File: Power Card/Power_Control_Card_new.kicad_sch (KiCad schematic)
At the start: 17 parts, among them J1 Conn_01x02_Pin, J4 Conn_01x04_Pin, Q1 IRF5305PbF, Q2 IRF5305PbF, U3 TSR2-2450, U4 TSR2-2433, U5 MCP9808_MSOP

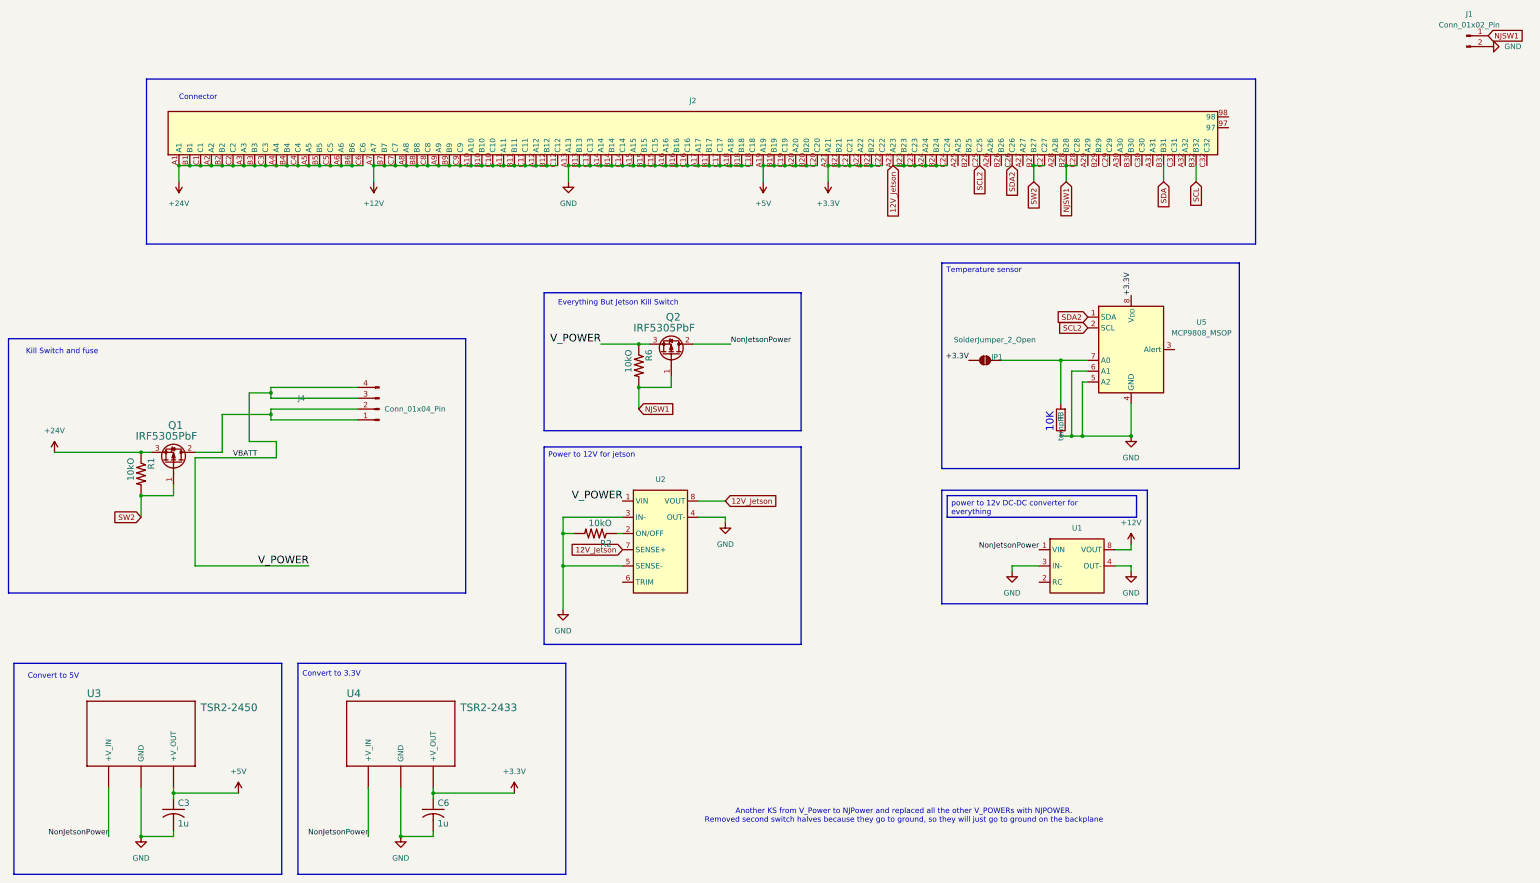
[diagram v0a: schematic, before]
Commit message: NJKS short
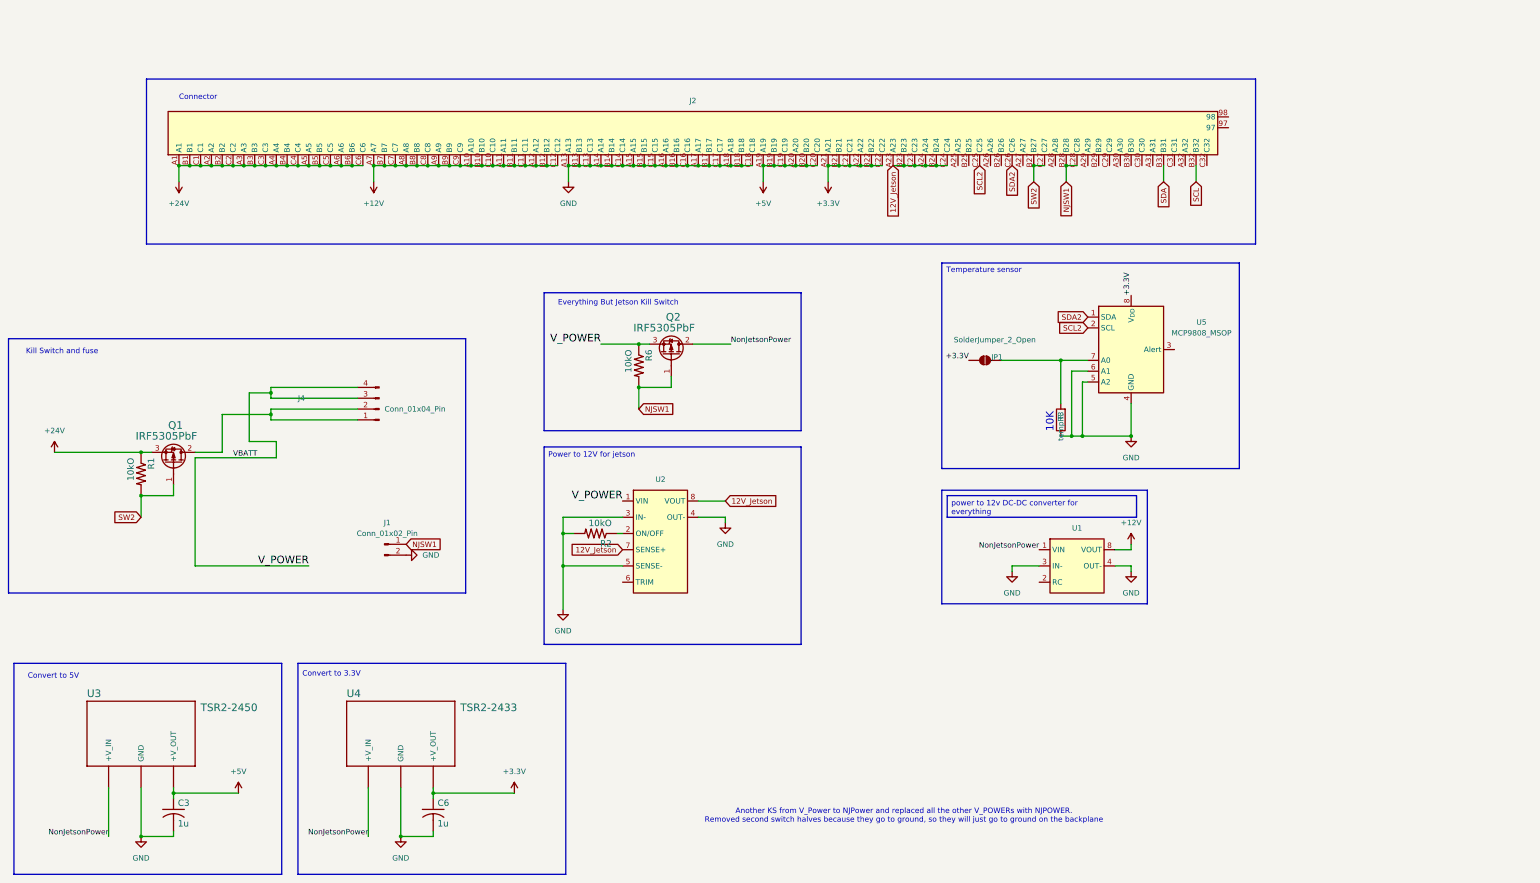
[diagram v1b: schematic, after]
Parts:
- J1: footprint (none) -> Connector_PinSocket_2.54mm:PinSocket_1x02_P2.54mm_Vertical
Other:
- moved on the sheet: J1
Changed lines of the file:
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@@
 	(global_label "NJSW1"
 		(shape input)
-		(at 369.57 60.96 0)
+		(at 115.57 180.34 0)
 		(fields_autoplaced yes)
 		(effects
@@
 		)
 		(property "Intersheetrefs" "${INTERSHEET_REFS}"
-			(at 378.7237 60.96 0)
+			(at 124.7237 180.34 0)
 			(effects
 				(font
@@
 	(symbol
 		(lib_id "Connector:Conn_01x02_Pin")
-		(at 364.49 60.96 0)
+		(at 110.49 180.34 0)
 		(unit 1)
 		(exclude_from_sim no)
@@
 		(fields_autoplaced yes)
 		(property "Reference" "J1"
-			(at 365.125 55.88 0)
+			(at 111.125 175.26 0)
 			(effects
 				(font
@@
 		)
 		(property "Value" "Conn_01x02_Pin"
-			(at 365.125 58.42 0)
-			(effects
-				(font
-					(size 1.27 1.27)
-				)
-			)
-		)
-		(property "Footprint" ""
-			(at 364.49 60.96 0)
+			(at 111.125 177.8 0)
+			(effects
+				(font
+					(size 1.27 1.27)
+				)
+			)
+		)
+		(property "Footprint" "Connector_PinSocket_2.54mm:PinSocket_1x02_P2.54mm_Vertical"
+			(at 110.49 180.34 0)
 			(effects
 				(font
@@
 		)
 		(property "Datasheet" "~"
-			(at 364.49 60.96 0)
+			(at 110.49 180.34 0)
 			(effects
 				(font
@@
 		)
 		(property "Description" "Generic connector, single row, 01x02, script generated"
-			(at 364.49 60.96 0)
+			(at 110.49 180.34 0)
 			(effects
 				(font
@@
 		(lib_name "GND_1")
 		(lib_id "power:GND")
-		(at 369.57 63.5 90)
+		(at 115.57 182.88 90)
 		(unit 1)
 		(exclude_from_sim no)
@@
 		(fields_autoplaced yes)
 		(property "Reference" "#PWR011"
-			(at 375.92 63.5 0)
+			(at 121.92 182.88 0)
 			(effects
 				(font
@@
 		)
 		(property "Value" "GND"
-			(at 373.38 63.4999 90)
+			(at 119.38 182.8799 90)
 			(effects
 				(font
@@
 		)
 		(property "Footprint" ""
-			(at 369.57 63.5 0)
+			(at 115.57 182.88 0)
 			(effects
 				(font
@@
 		)
 		(property "Datasheet" ""
-			(at 369.57 63.5 0)
+			(at 115.57 182.88 0)
 			(effects
 				(font
@@
 		)
 		(property "Description" "Power symbol creates a global label with name \"GND\" , ground"
-			(at 369.57 63.5 0)
-			(effects
-				(font
+			(at 115.57 182.88 0)
+			(effects
+				(font

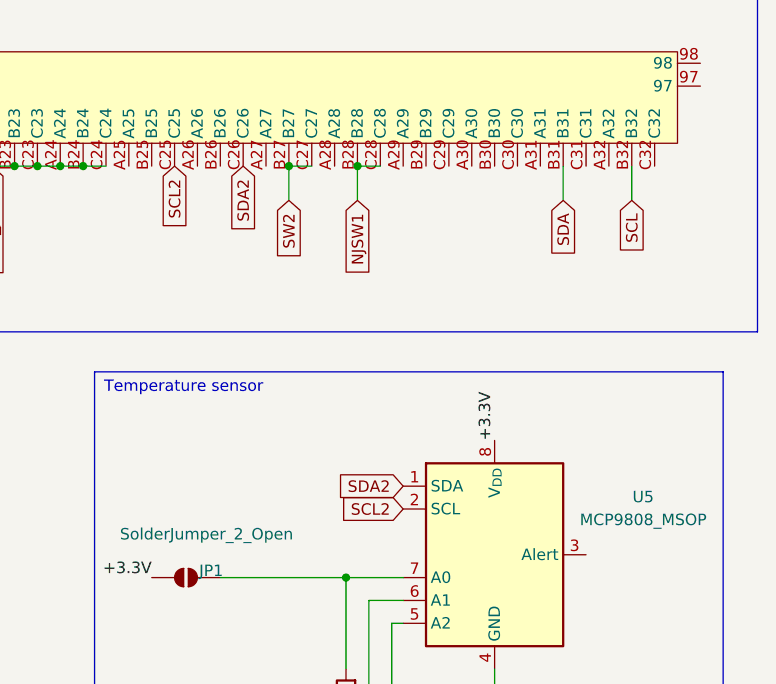
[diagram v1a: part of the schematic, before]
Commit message: Fixed the i2c line
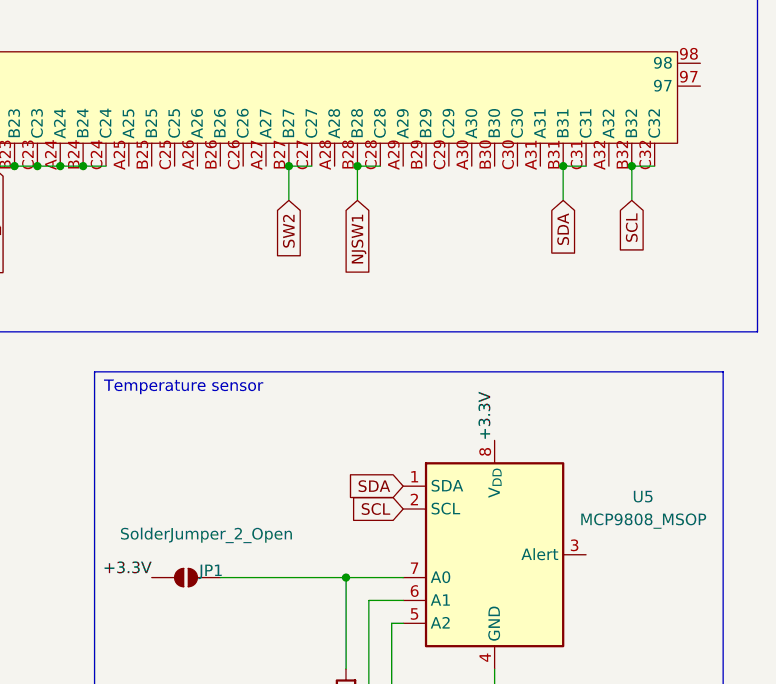
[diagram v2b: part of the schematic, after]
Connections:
- net SCL: now also J2.C32, U5.2 (SCL)
- net SDA: now also J2.C31, U5.1 (SDA)
- net SCL2: no longer names the net of J2.C25
- net SCL2: no longer U5.2 (SCL)
- net SDA2: no longer names the net of J2.C26
- net SDA2: no longer U5.1 (SDA)
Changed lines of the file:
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@@
+	)
+	(junction
+		(at 300.99 91.44)
+		(diameter 0)
+		(color 0 0 0 0)
 	)
 	(junction
@@
 	)
 	(junction
+		(at 293.37 91.44)
+		(diameter 0)
+		(color 0 0 0 0)
+	)
+	(junction
 		(at 274.32 154.94)
 		(diameter 0)
@@
 	(wire
 		(pts
+			(xy 300.99 91.44) (xy 303.53 91.44)
+		)
+		(stroke
+			(width 0)
+			(type default)
+		)
+	)
+	(wire
+		(pts
 			(xy 269.24 154.94) (xy 271.78 154.94)
+		)
+		(stroke
+			(width 0)
+			(type default)
+		)
+	)
+	(wire
+		(pts
+			(xy 293.37 91.44) (xy 295.91 91.44)
 		)
 		(stroke
@@
 	(global_label "SDA"
 		(shape input)
+		(at 275.59 127 180)
+		(fields_autoplaced yes)
+		(effects
+			(font
+				(size 1.27 1.27)
+			)
+			(justify right)
+		)
+		(property "Intersheetrefs" "${INTERSHEET_REFS}"
+			(at 269.0367 127 0)
+			(effects
+				(font
+					(size 1.27 1.27)
+				)
+				(justify right)
+				(hide yes)
+			)
+		)
+	)
+	(global_label "SDA"
+		(shape input)
 		(at 293.37 95.25 270)
 		(fields_autoplaced yes)
@@
 		)
 	)
-	(global_label "SDA2"
-		(shape input)
-		(at 275.59 127 180)
-		(fields_autoplaced yes)
-		(effects
-			(font
-				(size 1.27 1.27)
-			)
-			(justify right)
-		)
-		(property "Intersheetrefs" "${INTERSHEET_REFS}"
-			(at 267.8272 127 0)
-			(effects
-				(font
-					(size 1.27 1.27)
-				)
-				(justify right)
-				(hide yes)
-			)
-		)
-	)
-	(global_label "SCL2"
-		(shape input)
-		(at 250.19 91.44 270)
-		(fields_autoplaced yes)
-		(effects
-			(font
-				(size 1.27 1.27)
-			)
-			(justify right)
-		)
-		(property "Intersheetrefs" "${INTERSHEET_REFS}"
-			(at 250.19 99.1423 90)
-			(effects
-				(font
-					(size 1.27 1.27)
-				)
-				(justify right)
-				(hide yes)
-			)
-		)
-	)
 	(global_label "SW2"
 		(shape input)
@@
 		)
 	)
-	(global_label "SCL2"
+	(global_label "SCL"
 		(shape input)
 		(at 275.59 129.54 180)
@@
 		)
 		(property "Intersheetrefs" "${INTERSHEET_REFS}"
-			(at 267.8877 129.54 0)
+			(at 269.0972 129.54 0)
 			(effects
 				(font
-					(size 1.27 1.27)
-				)
-				(justify right)
-				(hide yes)
-			)
-		)
-	)
-	(global_label "SDA2"
-		(shape input)
-		(at 257.81 91.44 270)
-		(fields_autoplaced yes)
-		(effects
-			(font
-				(size 1.27 1.27)
-			)
-			(justify right)
-		)
-		(property "Intersheetrefs" "${INTERSHEET_REFS}"
-			(at 257.81 99.2028 90)
-			(effects
-				(font
